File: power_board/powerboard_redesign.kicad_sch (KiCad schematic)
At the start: 17 parts, among them J1 282834-2, J2 282834-2, J3 282834-2, J4 282834-2, U1 PDQ30-Q24-D12-D

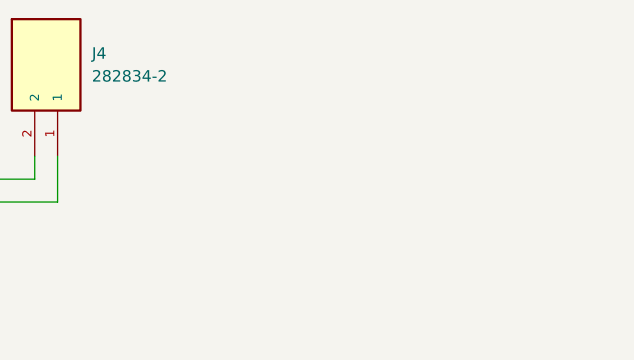
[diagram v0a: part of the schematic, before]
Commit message: Added BM06B-SRSS-TB to Schematic
No wires yet, need to know LiDAR module pins
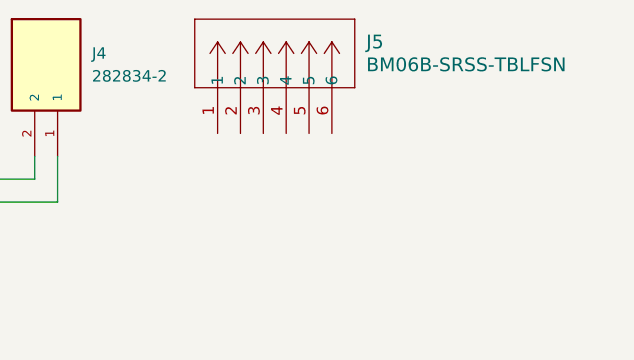
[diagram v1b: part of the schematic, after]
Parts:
- added J5: BM06B-SRSS-TBLFSN, F1TenthPowerBoard:CONN_BM06B-SRSS-TB_JST, symbol CONN_BM06B-SRSS-TB_JST:BM06B-SRSS-TBLFSN
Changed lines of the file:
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@@
+	)
+	(symbol
+		(lib_id "CONN_BM06B-SRSS-TB_JST:BM06B-SRSS-TBLFSN")
+		(at 241.3 50.8 90)
+		(unit 1)
+		(exclude_from_sim no)
+		(in_bom yes)
+		(on_board yes)
+		(dnp no)
+		(fields_autoplaced yes)
+		(property "Reference" "J5"
+			(at 257.81 40.6399 90)
+			(effects
+				(font
+					(size 1.524 1.524)
+				)
+				(justify right)
+			)
+		)
+		(property "Value" "BM06B-SRSS-TBLFSN"
+			(at 257.81 43.1799 90)
+			(effects
+				(font
+					(size 1.524 1.524)
+				)
+				(justify right)
+			)
+		)
+		(property "Footprint" "F1TenthPowerBoard:CONN_BM06B-SRSS-TB_JST"
+			(at 241.3 50.8 0)
+			(effects
+				(font
+					(size 1.27 1.27)
+					(italic yes)
+				)
+				(hide yes)
+			)
+		)
+		(property "Datasheet" "BM06B-SRSS-TBLFSN"
+			(at 241.3 50.8 0)
+			(effects
+				(font
+					(size 1.27 1.27)
+					(italic yes)
+				)
+				(hide yes)
+			)
+		)
+		(property "Description" ""
+			(at 241.3 50.8 0)
+			(effects
+				(font
+					(size 1.27 1.27)
+				)
+				(hide yes)
+			)
+		)
+		(pin "4"
+		)
+		(pin "3"
+		)
+		(pin "2"
+		)
+		(pin "6"
+		)
+		(pin "1"
+		)
+		(pin "5"
+		)
+		(instances
+			(project ""
+				(path "/730a7e3b-debe-415e-92d1-0c8950d2c05d"
+					(reference "J5")
+					(unit 1)
+				)
+			)
+		)
 	)
 	(symbol

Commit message: Adjusted other parts to use Project Specific Library Paths
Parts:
- J1, J2, J3, J4: footprint Library3:TE_282834-2 -> F1TenthPowerBoard:TE_282834-2
- S1: footprint Library2:SW_100SP1T1B4M2QE -> F1TenthPowerBoard:SW_100SP1T1B4M2QE
- U1: footprint Library:CONV_PDQ30-Q24-D12-D -> F1TenthPowerBoard:CONV_PDQ30-Q24-D12-D
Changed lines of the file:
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@@
 			)
 		)
-		(property "Footprint" "Library3:TE_282834-2"
+		(property "Footprint" "F1TenthPowerBoard:TE_282834-2"
 			(at 179.07 45.72 0)
 			(effects
@@
 			)
 		)
-		(property "Footprint" "Library3:TE_282834-2"
+		(property "Footprint" "F1TenthPowerBoard:TE_282834-2"
 			(at 220.98 45.72 0)
 			(effects
@@
 			)
 		)
-		(property "Footprint" "Library3:TE_282834-2"
+		(property "Footprint" "F1TenthPowerBoard:TE_282834-2"
 			(at 118.11 48.26 0)
 			(effects
@@
 			)
 		)
-		(property "Footprint" "Library2:SW_100SP1T1B4M2QE"
+		(property "Footprint" "F1TenthPowerBoard:SW_100SP1T1B4M2QE"
 			(at 76.2 88.9 0)
 			(effects
@@
 			)
 		)
-		(property "Footprint" "Library3:TE_282834-2"
+		(property "Footprint" "F1TenthPowerBoard:TE_282834-2"
 			(at 200.66 45.72 0)
 			(effects
@@
 			)
 		)
-		(property "Footprint" "Library:CONV_PDQ30-Q24-D12-D"
+		(property "Footprint" "F1TenthPowerBoard:CONV_PDQ30-Q24-D12-D"
 			(at 139.7 96.52 0)
 			(effects
